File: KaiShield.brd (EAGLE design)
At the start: 68.6 x 53.3 mm, 35 parts, among them IC1 MC33269ST-3.3T3, IC2 MCP1700-3302E/TO-ND

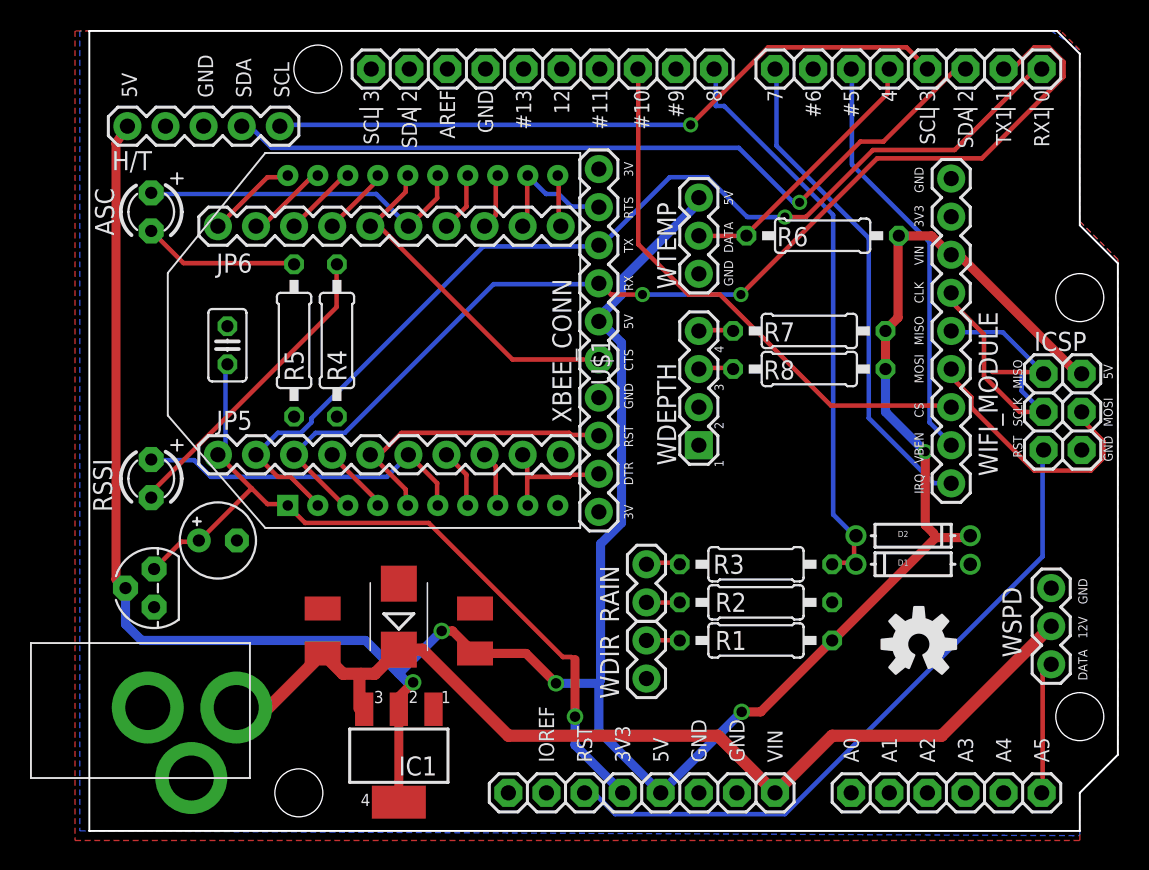
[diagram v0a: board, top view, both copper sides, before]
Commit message: Updated KaiShield board and added two more sensors. Now this is the main board instead of just a station board :D.
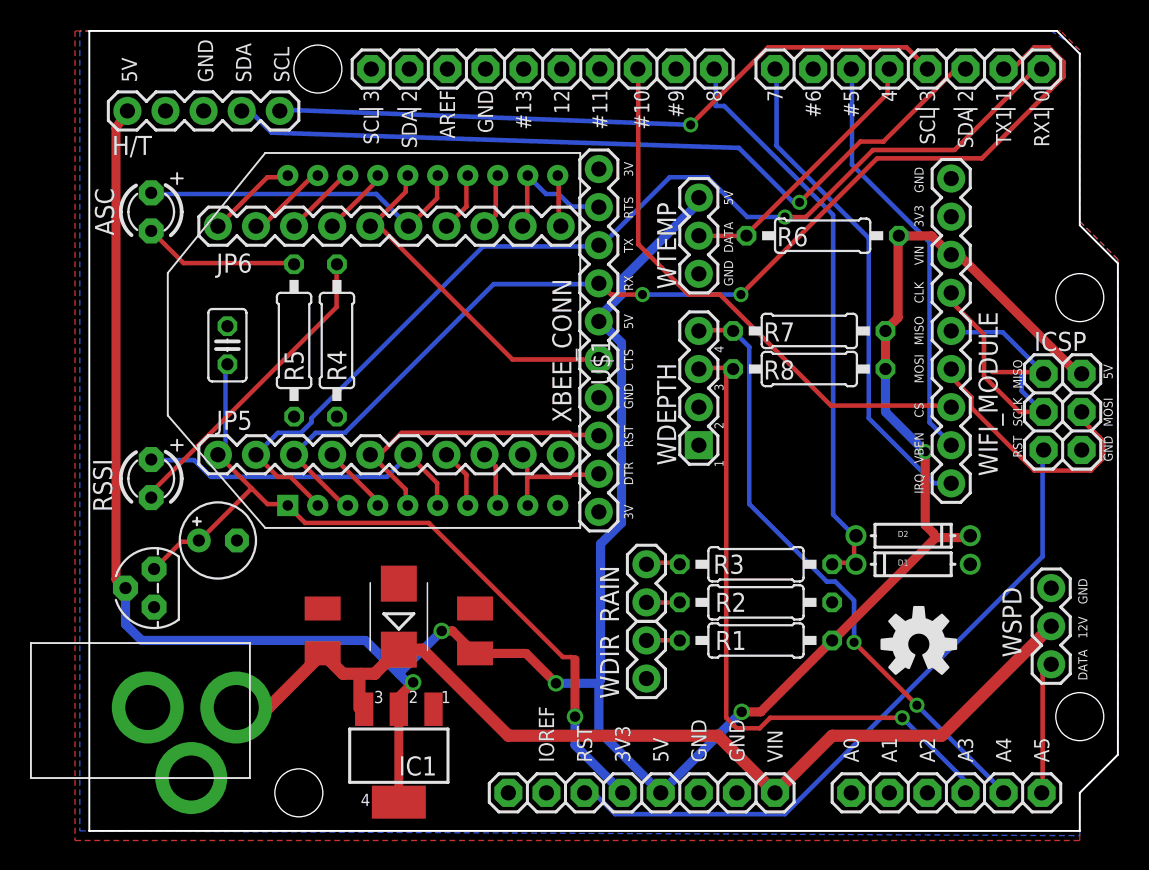
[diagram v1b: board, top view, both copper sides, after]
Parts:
- moved H/T 1.02 mm to (2.54, 48.0)
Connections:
- removed net N$11: R7.1, WDEPTH.4
- removed net N$12: R8.1, WDEPTH.3
- net A3: now also R8.1, WDEPTH.3
- net A4: now also R7.1, WDEPTH.4
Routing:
- net A3: track 0.00 -> 45.1 mm, vias 0 -> 1
- net A4: track 0.00 -> 40.9 mm, vias 0 -> 2
- net N$12: track 2.40 -> 0.00 mm
- net N$11: track 2.35 -> 0.00 mm
- net +5V: track 190.9 -> 192.0 mm
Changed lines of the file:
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@@
 <setting verticaltext="up"/>
 </settings>
-<grid distance="12.5" unitdist="mil" unit="mil" style="lines" multiple="1" display="yes" altdistance="0.025" altunitdist="inch" altunit="inch"/>
+<grid distance="5" unitdist="mil" unit="mil" style="lines" multiple="1" display="yes" altdistance="0.025" altunitdist="inch" altunit="inch"/>
 <layers>
 <layer number="1" name="Top" color="4" fill="1" visible="yes" active="yes"/>
@@
 <board>
 <plain>
-<text x="13.335" y="48.895" size="1.016" layer="21" ratio="7" rot="R90">SCL</text>
-<text x="10.795" y="48.895" size="1.016" layer="21" ratio="7" rot="R90">SDA</text>
-<text x="8.255" y="48.895" size="1.016" layer="21" ratio="7" rot="R90">GND</text>
-<text x="3.175" y="48.895" size="1.016" layer="21" ratio="7" rot="R90">5V</text>
+<text x="13.335" y="49.911" size="1.016" layer="21" ratio="7" rot="R90">SCL</text>
+<text x="10.795" y="49.911" size="1.016" layer="21" ratio="7" rot="R90">SDA</text>
+<text x="8.255" y="49.911" size="1.016" layer="21" ratio="7" rot="R90">GND</text>
+<text x="3.175" y="49.911" size="1.016" layer="21" ratio="7" rot="R90">5V</text>
 <text x="66.548" y="12.827" size="0.6096" layer="21" ratio="7" rot="R90">12V</text>
 <text x="66.548" y="15.113" size="0.6096" layer="21" ratio="7" rot="R90">GND</text>
@@
 </element>
 <element name="U$3" library="Kai" package="KAI_LOGO" value="KAI_LOGO" x="58.7375" y="18.3515" rot="MR0"/>
-<element name="H/T" library="SparkFun-Connectors" package="1X05" value="" x="2.54" y="46.99" smashed="yes">
-<attribute name="NAME" x="1.5113" y="44.0563" size="1.27" layer="25" ratio="10"/>
-<attribute name="VALUE" x="1.27" y="43.815" size="1.27" layer="27"/>
+<element name="H/T" library="SparkFun-Connectors" package="1X05" value="" x="2.54" y="48.006" smashed="yes">
+<attribute name="NAME" x="1.5113" y="45.0723" size="1.27" layer="25" ratio="10"/>
+<attribute name="VALUE" x="1.27" y="44.831" size="1.27" layer="27"/>
 </element>
 <element name="IC2" library="adafruit" package="TO92" value="MCP1700-3302E/TO-ND" x="4.318" y="16.1925" smashed="yes" rot="R90"/>
@@
 <contactref element="U$2" pad="D3SCL"/>
 <contactref element="H/T" pad="5"/>
-<wire x1="40.0939" y1="47.0789" x2="12.7127" y2="47.0789" width="0.3048" layer="16"/>
+<wire x1="40.0939" y1="47.0789" x2="12.7127" y2="48.0949" width="0.3048" layer="16"/>
 <wire x1="45.2628" y1="52.2478" x2="40.0939" y2="47.0789" width="0.3048" layer="1"/>
 <wire x1="54.483" y1="52.2478" x2="45.2628" y2="52.2478" width="0.3048" layer="1"/>
 <wire x1="55.88" y1="50.8508" x2="54.483" y2="52.2478" width="0.3048" layer="1"/>
-<wire x1="12.7127" y1="47.0789" x2="12.7" y2="46.99" width="0.3048" layer="16"/>
+<wire x1="12.7127" y1="48.0949" x2="12.7" y2="48.006" width="0.3048" layer="16"/>
 <wire x1="55.88" y1="50.8508" x2="55.88" y2="50.8" width="0.3048" layer="1"/>
 <via x="40.0939" y="47.0789" extent="1-16" drill="0.6096"/>
@@
 <contactref element="U$2" pad="D2SDA"/>
 <contactref element="H/T" pad="4"/>
-<wire x1="10.7569" y1="46.9392" x2="10.1981" y2="46.9392" width="0.3048" layer="16"/>
-<wire x1="12.1539" y1="45.5422" x2="10.7569" y2="46.9392" width="0.3048" layer="16"/>
-<wire x1="43.307" y1="45.5422" x2="12.1539" y2="45.5422" width="0.3048" layer="16"/>
-<wire x1="10.1981" y1="46.9392" x2="10.16" y2="46.99" width="0.3048" layer="16"/>
+<wire x1="10.7569" y1="47.9552" x2="10.1981" y2="47.9552" width="0.3048" layer="16"/>
+<wire x1="12.1539" y1="46.5582" x2="10.7569" y2="47.9552" width="0.3048" layer="16"/>
+<wire x1="43.307" y1="45.5422" x2="12.1539" y2="46.5582" width="0.3048" layer="16"/>
+<wire x1="10.1981" y1="47.9552" x2="10.16" y2="48.006" width="0.3048" layer="16"/>
 <wire x1="58.3946" y1="50.7111" x2="58.42" y2="50.8" width="0.3048" layer="1"/>
 <wire x1="57.6961" y1="50.7111" x2="58.2549" y2="50.7111" width="0.3048" layer="1"/>
@@
 <wire x1="2.413" y1="16.1925" x2="2.3495" y2="16.1925" width="0.6096" layer="1"/>
 <wire x1="2.3495" y1="16.1925" x2="1.778" y2="16.764" width="0.6096" layer="1"/>
-<wire x1="1.778" y1="16.764" x2="1.778" y2="45.847" width="0.6096" layer="1"/>
-<wire x1="1.778" y1="45.847" x2="2.54" y2="46.99" width="0.6096" layer="1"/>
+<wire x1="1.778" y1="16.764" x2="1.778" y2="46.863" width="0.6096" layer="1"/>
+<wire x1="1.778" y1="46.863" x2="2.54" y2="48.006" width="0.6096" layer="1"/>
 <wire x1="38.1" y1="2.54" x2="43.4975" y2="7.9375" width="0.6096" layer="16"/>
 <via x="43.4975" y="7.9375" extent="1-16" drill="0.7"/>
@@
 <signal name="A3">
 <contactref element="U$2" pad="A3"/>
+<contactref element="WDEPTH" pad="3"/>
+<contactref element="R8" pad="1"/>
+<wire x1="40.6527" y1="30.8737" x2="42.8879" y2="30.8737" width="0.3048" layer="1"/>
+<wire x1="42.8879" y1="30.8737" x2="42.926" y2="30.7975" width="0.3048" layer="1"/>
+<wire x1="40.6527" y1="30.8737" x2="40.64" y2="30.7975" width="0.3048" layer="1"/>
+<wire x1="58.3946" y1="3.3528" x2="58.3946" y2="2.6543" width="0.3048" layer="16"/>
+<wire x1="54.2036" y1="7.5438" x2="58.3946" y2="3.3528" width="0.3048" layer="16"/>
+<wire x1="45.4025" y1="7.5438" x2="54.2036" y2="7.5438" width="0.3048" layer="1"/>
+<wire x1="44.704" y1="6.8453" x2="45.4025" y2="7.5438" width="0.3048" layer="1"/>
+<wire x1="43.1673" y1="6.8453" x2="44.704" y2="6.8453" width="0.3048" layer="1"/>
+<wire x1="42.4688" y1="7.5438" x2="43.1673" y2="6.8453" width="0.3048" layer="1"/>
+<wire x1="42.4688" y1="30.734" x2="42.4688" y2="7.5438" width="0.3048" layer="1"/>
+<wire x1="58.3946" y1="2.6543" x2="58.42" y2="2.54" width="0.3048" layer="16"/>
+<wire x1="42.4688" y1="30.734" x2="42.926" y2="30.7975" width="0.3048" layer="1"/>
+<via x="54.2036" y="7.5438" extent="1-16" drill="0.6096"/>
 </signal>
 <signal name="D4">
@@
 <signal name="A4">
 <contactref element="U$2" pad="A4"/>
+<contactref element="WDEPTH" pad="4"/>
+<contactref element="R7" pad="1"/>
+<wire x1="40.6527" y1="33.3883" x2="42.8879" y2="33.3883" width="0.3048" layer="1"/>
+<wire x1="42.8879" y1="33.3883" x2="42.926" y2="33.3375" width="0.3048" layer="1"/>
+<wire x1="40.6527" y1="33.3883" x2="40.64" y2="33.3375" width="0.3048" layer="1"/>
+<wire x1="55.1815" y1="8.382" x2="60.9092" y2="2.6543" width="0.3048" layer="16"/>
+<wire x1="50.9905" y1="12.573" x2="55.1815" y2="8.382" width="0.3048" layer="1"/>
+<wire x1="50.9905" y1="15.367" x2="50.9905" y2="12.573" width="0.3048" layer="16"/>
+<wire x1="49.7332" y1="16.6243" x2="50.9905" y2="15.367" width="0.3048" layer="16"/>
+<wire x1="49.1744" y1="16.6243" x2="49.7332" y2="16.6243" width="0.3048" layer="16"/>
+<wire x1="44.0055" y1="21.7932" x2="49.1744" y2="16.6243" width="0.3048" layer="16"/>
+<wire x1="44.0055" y1="32.2707" x2="44.0055" y2="21.7932" width="0.3048" layer="16"/>
+<wire x1="43.0276" y1="33.2486" x2="44.0055" y2="32.2707" width="0.3048" layer="16"/>
+<wire x1="60.9092" y1="2.6543" x2="60.96" y2="2.54" width="0.3048" layer="16"/>
+<wire x1="43.0276" y1="33.2486" x2="42.926" y2="33.3375" width="0.3048" layer="16"/>
+<via x="55.1815" y="8.382" extent="1-16" drill="0.6096"/>
+<via x="50.9905" y="12.573" extent="1-16" drill="0.6096"/>
 </signal>
 <signal name="D0">
@@
 <wire x1="26.4033" y1="25.0063" x2="26.3525" y2="25.0825" width="0.3048" layer="1"/>
 </signal>
-<signal name="N$11">
-<contactref element="WDEPTH" pad="4"/>
-<contactref element="R7" pad="1"/>
-<wire x1="40.6527" y1="33.3883" x2="42.8879" y2="33.3883" width="0.3048" layer="1"/>
-<wire x1="42.8879" y1="33.3883" x2="42.926" y2="33.3375" width="0.3048" layer="1"/>
-<wire x1="40.6527" y1="33.3883" x2="40.64" y2="33.3375" width="0.3048" layer="1"/>
-</signal>
-<signal name="N$12">
-<contactref element="WDEPTH" pad="3"/>
-<contactref element="R8" pad="1"/>
-<wire x1="40.6527" y1="30.8737" x2="42.8879" y2="30.8737" width="0.3048" layer="1"/>
-<wire x1="42.8879" y1="30.8737" x2="42.926" y2="30.7975" width="0.3048" layer="1"/>
-<wire x1="40.6527" y1="30.8737" x2="40.64" y2="30.7975" width="0.3048" layer="1"/>
-</signal>
 </signals>

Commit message: updated KaiShield with the new power ic foot print DPAK
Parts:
- removed C10: 10u, rcl:SMC_B
- removed IC1: MC33269ST-3.3T3, linear:SOT223
- added C4: 10u, rcl:SMC_B
- added IC3: MC33269D-5.0, linear:DPACK
- moved D3 7.05 mm to (20.6, 7.24)
- moved C3 6.18 mm to (24.7, 7.24)
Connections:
- net +12V: now also C4.+, IC3.3; no longer C10.+, IC1.3
- net +5V: now also IC3.2; no longer IC1.2, IC1.4
- net GND: now also C4.-, IC3.1; no longer C10.-, IC1.1
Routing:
- net +12V: track 68.3 -> 76.3 mm
- net 3V3: track 54.7 -> 57.2 mm
- net +5V: track 192.0 -> 191.1 mm, vias 5 -> 4
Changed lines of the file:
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@@
 <setting verticaltext="up"/>
 </settings>
-<grid distance="5" unitdist="mil" unit="mil" style="lines" multiple="1" display="yes" altdistance="0.025" altunitdist="inch" altunit="inch"/>
+<grid distance="10" unitdist="mil" unit="mil" style="lines" multiple="1" display="yes" altdistance="0.025" altunitdist="inch" altunit="inch"/>
 <layers>
 <layer number="1" name="Top" color="4" fill="1" visible="yes" active="yes"/>
@@
 </element>
 <element name="IC2" library="adafruit" package="TO92" value="MCP1700-3302E/TO-ND" x="4.318" y="16.1925" smashed="yes" rot="R90"/>
-<element name="D3" library="diode" package="SMB" value="M7" x="20.6375" y="14.2875" smashed="yes" rot="R90"/>
-<element name="C10" library="rcl" package="SMC_B" value="10u" x="15.5575" y="13.335" smashed="yes" rot="R90"/>
-<element name="C3" library="rcl" package="SMC_B" value="10u" x="25.7175" y="13.335" smashed="yes" rot="R90"/>
-<element name="IC1" library="linear" package="SOT223" value="MC33269ST-3.3T3" x="20.6375" y="5.0165" smashed="yes" rot="R180">
-<attribute name="NAME" x="23.1775" y="4.9657" size="1.27" layer="25" rot="R180"/>
-</element>
+<element name="D3" library="diode" package="SMB" value="M7" x="20.574" y="7.239" smashed="yes" rot="R90"/>
+<element name="C4" library="rcl" package="SMC_B" value="10u" x="16.7005" y="7.239" smashed="yes" rot="R90"/>
+<element name="C3" library="rcl" package="SMC_B" value="10u" x="24.7015" y="7.239" smashed="yes" rot="R90"/>
 <element name="U$4" library="adafruit" package="PJ-102A" value="2.1MMJACKTHM" x="0.508" y="8.128" rot="R90"/>
 <element name="WDEPTH" library="SparkFun-Connectors" package="1X04" value="" x="40.64" y="25.7175" smashed="yes" rot="R90">
@@
 <attribute name="VALUE" x="45.7454" y="30.1625" size="1.27" layer="27" ratio="10"/>
 </element>
+<element name="IC3" library="linear" package="DPACK" value="MC33269D-5.0" x="22.606" y="15.24" rot="R90"/>
 </elements>
 <signals>
@@
 <contactref element="IC2" pad="1"/>
 <contactref element="D3" pad="A"/>
-<contactref element="C10" pad="-"/>
+<contactref element="C4" pad="-"/>
 <contactref element="C3" pad="-"/>
-<contactref element="IC1" pad="1"/>
 <contactref element="U$4" pad="RING"/>
 <contactref element="U$4" pad="RING_SW"/>
@@
 <contactref element="WDEPTH" pad="1"/>
 <contactref element="WDEPTH" pad="2"/>
+<contactref element="IC3" pad="1"/>
 </signal>
 <signal name="TX">
@@
 <wire x1="10.82675" y1="22.84095" x2="7.4041" y2="19.4183" width="0.3048" layer="1"/>
 <wire x1="7.4041" y1="19.4183" x2="7.3025" y2="19.3675" width="0.3048" layer="1"/>
-<wire x1="31.5722" y1="11.5951" x2="32.131" y2="11.5951" width="0.3048" layer="1"/>
-<wire x1="22.6314" y1="20.5359" x2="31.5722" y2="11.5951" width="0.3048" layer="1"/>
-<wire x1="14.3891" y1="20.5359" x2="22.6314" y2="20.5359" width="0.3048" layer="1"/>
+<wire x1="14.3891" y1="20.5359" x2="27.3812" y2="20.5359" width="0.3048" layer="1"/>
 <wire x1="13.2715" y1="21.6535" x2="14.3891" y2="20.5359" width="0.3048" layer="1"/>
 <wire x1="32.131" y1="11.5951" x2="32.385" y2="11.43" width="0.3048" layer="1"/>
 <wire x1="13.2715" y1="21.6535" x2="13.2325" y2="21.7025" width="0.3048" layer="1"/>
+<wire x1="32.131" y1="15.7861" x2="32.131" y2="11.5951" width="0.3048" layer="1"/>
+<wire x1="27.3812" y1="20.5359" x2="32.131" y2="15.7861" width="0.3048" layer="1"/>
 </signal>
 <signal name="+5V" class="2">
@@
 <contactref element="IC2" pad="2"/>
 <contactref element="C3" pad="+"/>
-<contactref element="IC1" pad="2"/>
-<contactref element="IC1" pad="4"/>
-<wire x1="20.6375" y1="10.4775" x2="23.495" y2="13.335" width="0.6096" layer="16"/>
-<via x="23.495" y="13.335" extent="1-16" drill="0.7"/>
-<wire x1="23.495" y1="13.335" x2="24.2175" y2="13.335" width="0.6096" layer="1"/>
-<wire x1="24.2175" y1="13.335" x2="25.7175" y2="11.835" width="0.6096" layer="1"/>
-<wire x1="25.7175" y1="11.835" x2="29.1225" y2="11.835" width="0.6096" layer="1"/>
-<wire x1="29.1225" y1="11.835" x2="31.115" y2="9.8425" width="0.6096" layer="1"/>
-<via x="31.115" y="9.8425" extent="1-16" drill="0.7"/>
-<wire x1="31.115" y1="9.8425" x2="33.9725" y2="9.8425" width="0.6096" layer="16"/>
 <wire x1="33.9725" y1="9.8425" x2="33.9725" y2="6.6675" width="0.6096" layer="16"/>
 <wire x1="33.9725" y1="6.6675" x2="38.1" y2="2.54" width="0.6096" layer="16"/>
-<wire x1="20.6375" y1="8.1153" x2="20.6375" y2="1.9175" width="0.6096" layer="1"/>
 <wire x1="2.413" y1="16.1925" x2="2.3495" y2="16.1925" width="0.6096" layer="1"/>
 <wire x1="2.3495" y1="16.1925" x2="1.778" y2="16.764" width="0.6096" layer="1"/>
@@
 <wire x1="2.413" y1="16.1925" x2="2.413" y2="13.7795" width="0.6096" layer="16"/>
 <wire x1="2.413" y1="13.7795" x2="3.4925" y2="12.7" width="0.6096" layer="16"/>
-<wire x1="3.4925" y1="12.7" x2="18.415" y2="12.7" width="0.6096" layer="16"/>
-<wire x1="18.415" y1="12.7" x2="20.6375" y2="10.4775" width="0.6096" layer="16"/>
-<wire x1="20.6375" y1="8.1153" x2="20.6375" y2="8.9535" width="0.6096" layer="1"/>
-<wire x1="20.6375" y1="8.9535" x2="21.59" y2="9.906" width="0.6096" layer="1"/>
-<via x="21.59" y="9.906" extent="1-16" drill="0.7"/>
-<wire x1="21.59" y1="9.906" x2="21.209" y2="9.906" width="0.6096" layer="16"/>
-<wire x1="21.209" y1="9.906" x2="20.6375" y2="10.4775" width="0.6096" layer="16"/>
 <contactref element="WTEMP" pad="3"/>
 <contactref element="R6" pad="1"/>
@@
 <wire x1="53.9242" y1="39.3954" x2="53.975" y2="39.6875" width="0.6096" layer="1"/>
 <wire x1="53.2257" y1="33.528" x2="53.086" y2="33.3375" width="0.6096" layer="1"/>
+<contactref element="IC3" pad="2"/>
+<wire x1="3.4925" y1="12.7" x2="14.986" y2="12.7" width="0.8128" layer="16"/>
+<wire x1="14.986" y1="12.7" x2="20.574" y2="7.366" width="0.8128" layer="16"/>
+<wire x1="20.574" y1="7.366" x2="22.86" y2="7.366" width="0.8128" layer="16"/>
+<via x="22.86" y="7.366" extent="1-16" drill="0.7"/>
+<wire x1="22.86" y1="7.366" x2="23.0745" y2="7.366" width="0.8128" layer="1"/>
+<wire x1="23.0745" y1="7.366" x2="24.7015" y2="5.739" width="0.8128" layer="1"/>
+<wire x1="33.9725" y1="9.8425" x2="25.5905" y2="9.8425" width="0.8128" layer="16"/>
+<wire x1="25.5905" y1="9.8425" x2="22.86" y2="7.366" width="0.8128" layer="16"/>
+<via x="14.986" y="12.7" extent="1-16" drill="0.7"/>
+<wire x1="14.986" y1="12.7" x2="16.002" y2="13.716" width="0.8128" layer="1"/>
+<wire x1="16.002" y1="13.716" x2="19.598" y2="13.716" width="0.8128" layer="1"/>
+<wire x1="19.598" y1="13.716" x2="20.106" y2="15.24" width="0.8128" layer="1"/>
 </signal>
 <signal name="X_RST">
@@
 <contactref element="U$2" pad="VIN"/>
 <contactref element="D3" pad="C"/>
-<contactref element="C10" pad="+"/>
-<contactref element="IC1" pad="3"/>
-<wire x1="18.0086" y1="8.1788" x2="18.3261" y2="8.1153" width="0.6096" layer="1"/>
-<wire x1="18.0975" y1="10.4775" x2="19.0275" y2="10.4775" width="0.8128" layer="1"/>
-<wire x1="19.0275" y1="10.4775" x2="20.6375" y2="12.0875" width="0.8128" layer="1"/>
-<wire x1="18.0086" y1="8.1788" x2="18.0086" y2="10.3886" width="0.8128" layer="1"/>
-<wire x1="18.0086" y1="10.3886" x2="18.0975" y2="10.4775" width="0.6096" layer="1"/>
-<wire x1="18.0975" y1="10.4775" x2="16.915" y2="10.4775" width="0.8128" layer="1"/>
-<wire x1="16.915" y1="10.4775" x2="15.5575" y2="11.835" width="0.8128" layer="1"/>
-<wire x1="20.6375" y1="12.0875" x2="22.2025" y2="12.0875" width="0.8128" layer="1"/>
-<wire x1="22.2025" y1="12.0875" x2="27.94" y2="6.35" width="0.8128" layer="1"/>
-<wire x1="27.94" y1="6.35" x2="41.91" y2="6.35" width="0.8128" layer="1"/>
+<contactref element="C4" pad="+"/>
 <wire x1="41.91" y1="6.35" x2="45.72" y2="2.54" width="0.8128" layer="1"/>
 <wire x1="45.72" y1="2.54" x2="49.53" y2="6.35" width="0.8128" layer="1"/>
@@
 <wire x1="56.8325" y1="6.35" x2="64.135" y2="13.6525" width="0.8128" layer="1"/>
 <contactref element="U$4" pad="TIP"/>
-<wire x1="9.798" y1="8.228" x2="11.9505" y2="8.228" width="0.8128" layer="1"/>
-<wire x1="11.9505" y1="8.228" x2="15.5575" y2="11.835" width="0.8128" layer="1"/>
+<contactref element="IC3" pad="3"/>
+<wire x1="41.91" y1="6.35" x2="29.8958" y2="6.35" width="0.8128" layer="1"/>
+<wire x1="29.8958" y1="6.35" x2="28.448" y2="6.35" width="0.8128" layer="1"/>
+<wire x1="28.448" y1="6.35" x2="25.908" y2="3.81" width="0.8128" layer="1"/>
+<wire x1="25.908" y1="3.81" x2="21.549" y2="3.81" width="0.8128" layer="1"/>
+<wire x1="21.549" y1="3.81" x2="20.574" y2="5.039" width="0.8128" layer="1"/>
+<wire x1="28.4988" y1="15.0876" x2="28.4988" y2="17.4625" width="0.6096" layer="1"/>
+<wire x1="29.8958" y1="13.6906" x2="28.4988" y2="15.0876" width="0.6096" layer="1"/>
+<wire x1="29.8958" y1="6.35" x2="29.8958" y2="13.6906" width="0.6096" layer="1"/>
+<wire x1="28.4988" y1="17.4625" x2="27.406" y2="17.52" width="0.6096" layer="1"/>
+<wire x1="20.574" y1="5.039" x2="17.4005" y2="5.039" width="0.8128" layer="1"/>
+<wire x1="17.4005" y1="5.039" x2="16.7005" y2="5.739" width="0.8128" layer="1"/>
+<wire x1="16.7005" y1="5.739" x2="16.359" y2="5.739" width="0.8128" layer="1"/>
+<wire x1="16.359" y1="5.739" x2="14.986" y2="7.112" width="0.8128" layer="1"/>
+<wire x1="14.986" y1="7.112" x2="10.914" y2="7.112" width="0.8128" layer="1"/>
+<wire x1="10.914" y1="7.112" x2="9.798" y2="8.228" width="0.8128" layer="1"/>
 </signal>
 <signal name="N$1">
